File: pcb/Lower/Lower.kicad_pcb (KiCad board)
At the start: 2 copper layers, 52 x 42 mm, 29 parts, among them J4 Conn_01x04, Q1 AO3401A, SW1 SW_Push_3PDT, U1 TL072

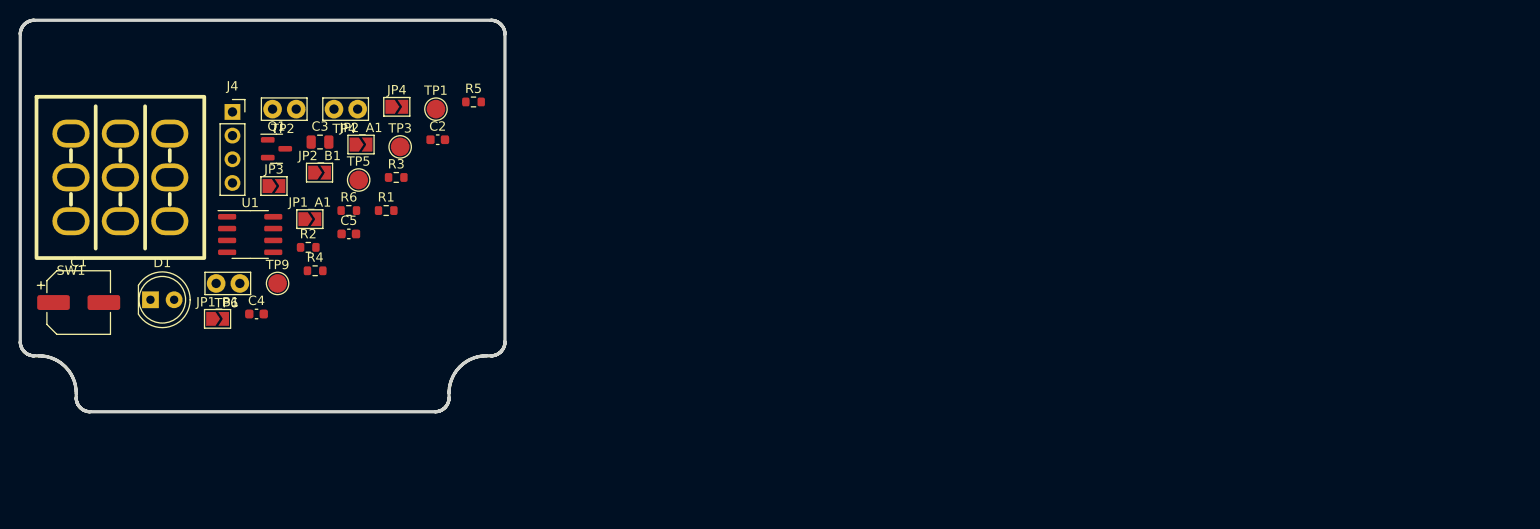
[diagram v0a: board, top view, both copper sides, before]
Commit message: [Lower] Design and add more footprints
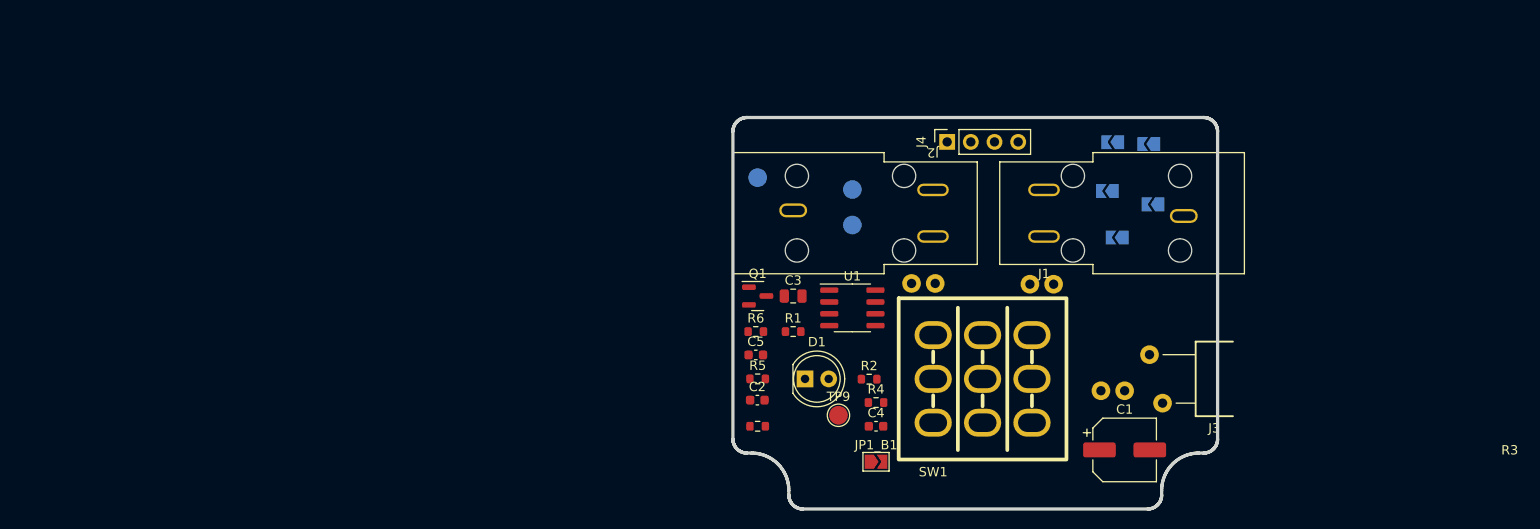
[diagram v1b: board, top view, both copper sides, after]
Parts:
- added J1: AudioJack3, MeineBib:Audio_Jack_PJ-602B, F.Cu at (250.2, 95.2)
- added J2: AudioJack3, MeineBib:Audio_Jack_PJ-602B, F.Cu at (208.3, 95.2)
- added J3: Barrel_Jack, MeineBib:DC_Barrel_Jack_Thinline_Wired_Standing, F.Cu at (251.5, 113.0)
- JP1_A1, JP2_A1, JP2_B1, JP3, JP4, TP1, TP2, TP3, TP4, TP5, TP6: moved to B.Cu
- moved C1 113.3 mm to (243.8, 120.7)
- moved SW1 95.0 mm to (228.6, 113.0)
- moved JP3 94.3 mm to (246.9, 94.3), turned to 180 degrees
- moved TP4 90.0 mm to (243.8, 114.3), turned to 180 degrees
- moved JP1_A1 86.6 mm to (243.0, 97.9), turned to 180 degrees
- moved TP2 85.9 mm to (236.2, 102.9), turned to 180 degrees
- moved JP2_B1 84.6 mm to (242.0, 92.9), turned to 180 degrees
- moved JP4 80.8 mm to (246.4, 87.8), turned to 180 degrees
- moved JP2_A1 80.7 mm to (242.6, 87.6), turned to 180 degrees
- moved TP6 77.1 mm to (223.5, 102.8), turned to 180 degrees
- moved J4 76.7 mm to (224.8, 87.6), turned to 90 degrees
- moved JP1_B1 72.3 mm to (217.2, 121.9)
- moved D1 70.7 mm to (209.6, 113.0)
- moved C4 67.5 mm to (217.2, 118.1)
- moved U1 65.1 mm to (214.6, 105.4)
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
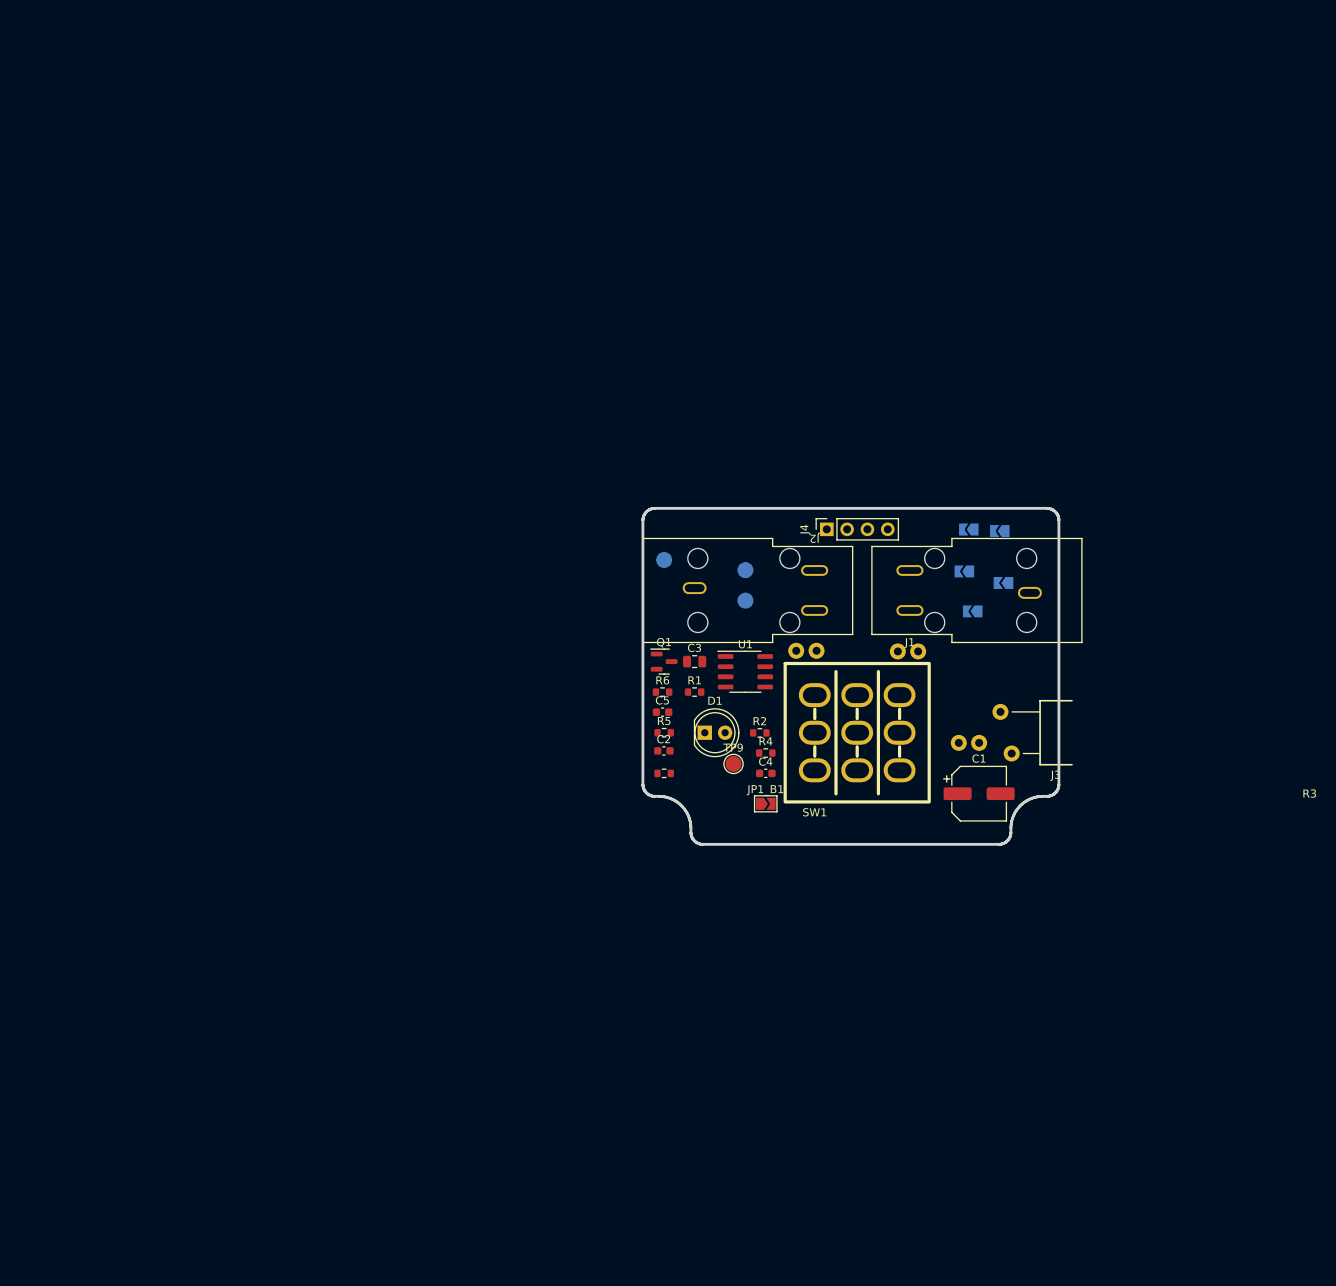
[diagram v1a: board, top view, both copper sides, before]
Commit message: [Lower] Start mechanical design
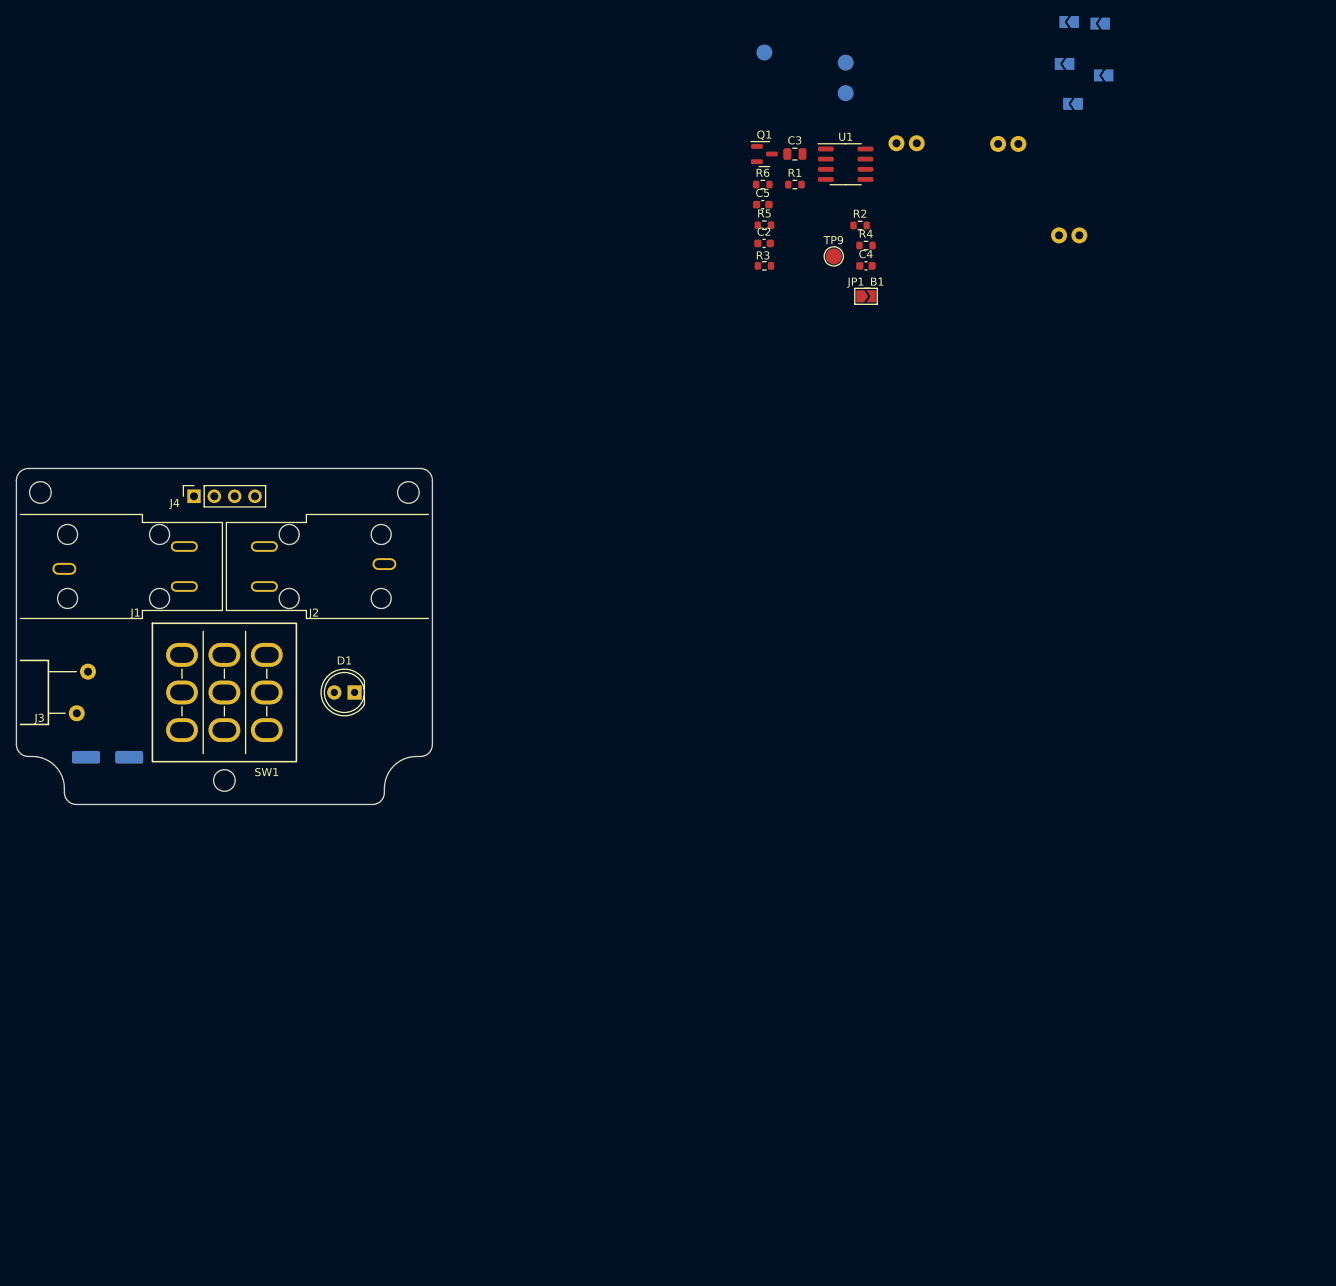
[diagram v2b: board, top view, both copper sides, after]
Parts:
- added MK2: Mounting_Hole, MeineBib:EigenesMountingHole_2.7mm_M2.5, F.Cu at (126.5, 83.0)
- added MK2: Mounting_Hole, MeineBib:EigenesMountingHole_2.7mm_M2.5, F.Cu at (172.5, 83.0)
- added MK2: Mounting_Hole, MeineBib:EigenesMountingHole_2.7mm_M2.5, F.Cu at (149.5, 119.0)
- C1, D1, J1, J2, J3, SW1: moved to B.Cu
- moved J3 124.1 mm to (127.5, 108.0), turned to 180 degrees
- moved J1 120.7 mm to (129.5, 92.2), turned to 180 degrees
- moved C1 109.0 mm to (134.9, 116.1), turned to 180 degrees
- moved SW1 79.3 mm to (149.5, 108.0), turned to 180 degrees
- moved J4 79.2 mm to (145.7, 83.5)
- moved C2 64.7 mm to (217.0, 51.9)
- moved JP1_B1 64.7 mm to (229.7, 58.5)
- moved JP2_B1 64.7 mm to (254.5, 29.4)
- moved JP4 64.7 mm to (259.0, 24.4)
- moved R1 64.7 mm to (220.8, 44.5)
- moved R2 64.7 mm to (229.0, 49.6)
- moved R6 64.7 mm to (216.8, 44.5)
- moved TP2 64.7 mm to (248.8, 39.4)
- moved TP9 64.7 mm to (225.7, 53.5)
- moved C3 64.7 mm to (220.8, 40.7)
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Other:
- outline, holes or cut-outs redrawn

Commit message: [Lower] Continue mechanical design
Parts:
- moved C5 50.9 mm to (170.1, 67.4)
- moved R6 50.9 mm to (170.1, 64.9)
- moved TP6 50.9 mm to (189.4, 59.7)
- moved JP4 50.9 mm to (212.3, 44.8)
- moved C2 50.9 mm to (170.3, 72.3)
- moved C3 50.9 mm to (174.1, 61.1)
- moved C4 50.9 mm to (183.0, 75.1)
- moved JP1_A1 50.9 mm to (208.9, 54.8)
- moved JP1_B1 50.9 mm to (183.0, 78.9)
- moved JP2_A1 50.9 mm to (208.4, 44.6)
- moved JP2_B1 50.9 mm to (207.9, 49.8)
- moved JP3 50.9 mm to (212.7, 51.3)
- moved Q1 50.9 mm to (170.3, 61.1)
- moved R1 50.9 mm to (174.1, 64.9)
- moved R2 50.9 mm to (182.3, 70.0)
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
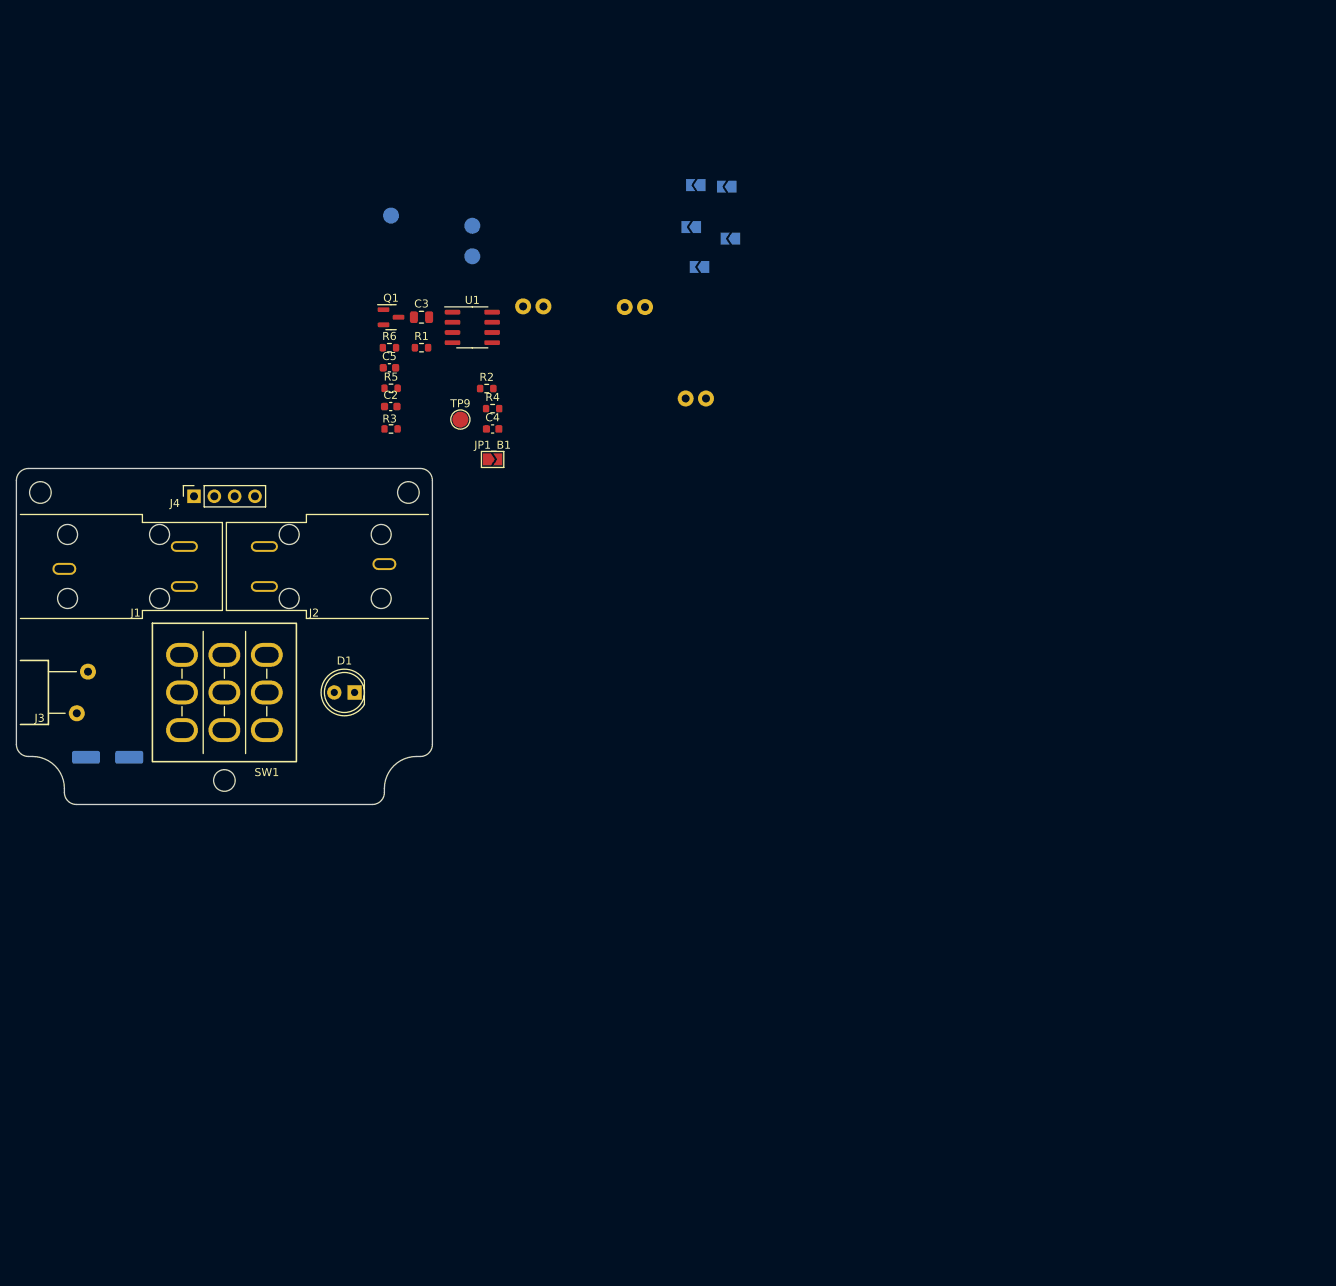
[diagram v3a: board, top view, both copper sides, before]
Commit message: [Lower] Fix some footprints 3D models
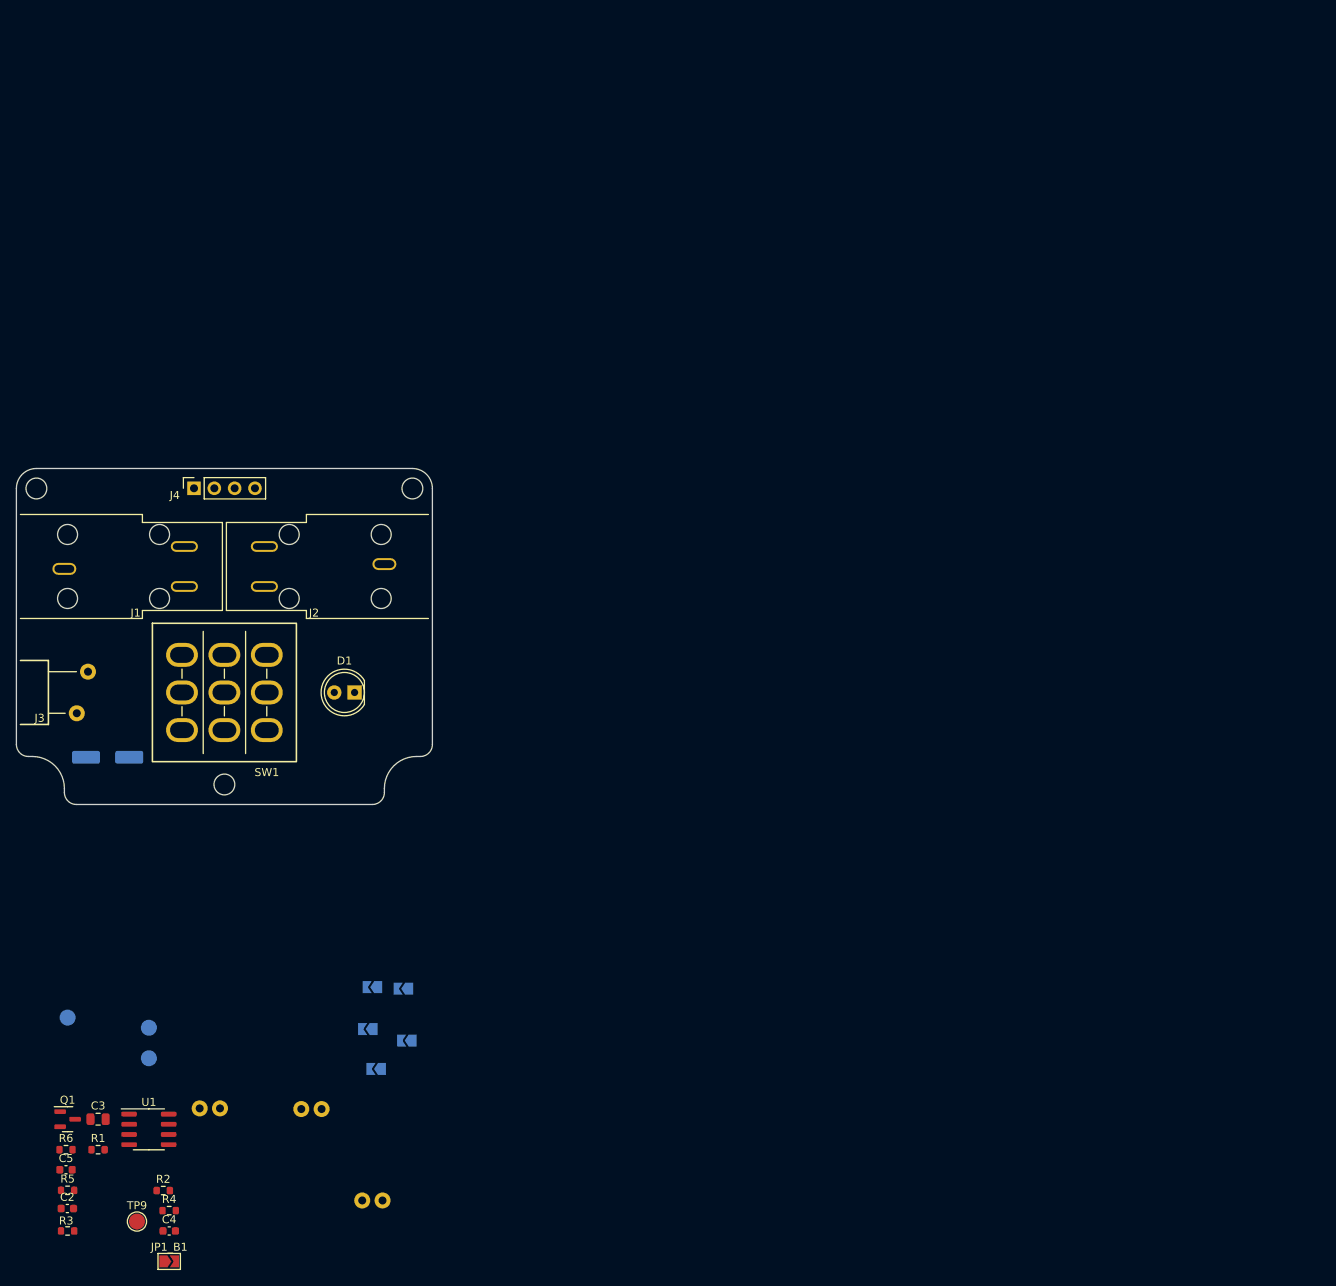
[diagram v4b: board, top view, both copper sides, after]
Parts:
- MK2 (x3): footprint MeineBib:EigenesMountingHole_2.7mm_M2.5 -> MeineBib:EigenesMountingHole_2.6mm_M2.5_Small
- moved JP2_A1 108.1 mm to (168.0, 144.8)
- moved U1 108.1 mm to (140.1, 162.6)
- moved C2 108.1 mm to (129.9, 172.5)
- moved C3 108.1 mm to (133.7, 161.3)
- moved C4 108.1 mm to (142.6, 175.3)
- moved JP1_A1 108.1 mm to (168.5, 155.1)
- moved JP1_B1 108.1 mm to (142.6, 179.1)
- moved JP4 108.1 mm to (171.9, 145.0)
- moved Q1 108.1 mm to (129.9, 161.3)
- moved R1 108.1 mm to (133.7, 165.2)
- moved R3 108.1 mm to (129.9, 175.3)
- moved R4 108.1 mm to (142.6, 172.8)
- moved R6 108.1 mm to (129.7, 165.2)
- moved TP4 108.1 mm to (169.3, 171.5)
- moved C5 108.1 mm to (129.7, 167.7)
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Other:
- outline, holes or cut-outs redrawn
